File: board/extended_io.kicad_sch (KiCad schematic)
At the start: 54 parts, among them J5 I2C_3V3, Q10 BC548, Q11 BC548, Q12 BC548, Q13 BC548, Q14 BC548, Q15 BC548, Q16 BC548, Q17 BC548, Q18 BC548, Q7 BC548, Q8 BC548, Q9 BC548, SW11 TD_A, SW12 TD_B, SW13 TD2_A, SW14 TD2_B, SW15 SW_DIP_x03, U10 MCP23008-xP, U11 CAT24C256, U12 MCP7940N-xP, U9 24LC1025, Y1 32.768kHz

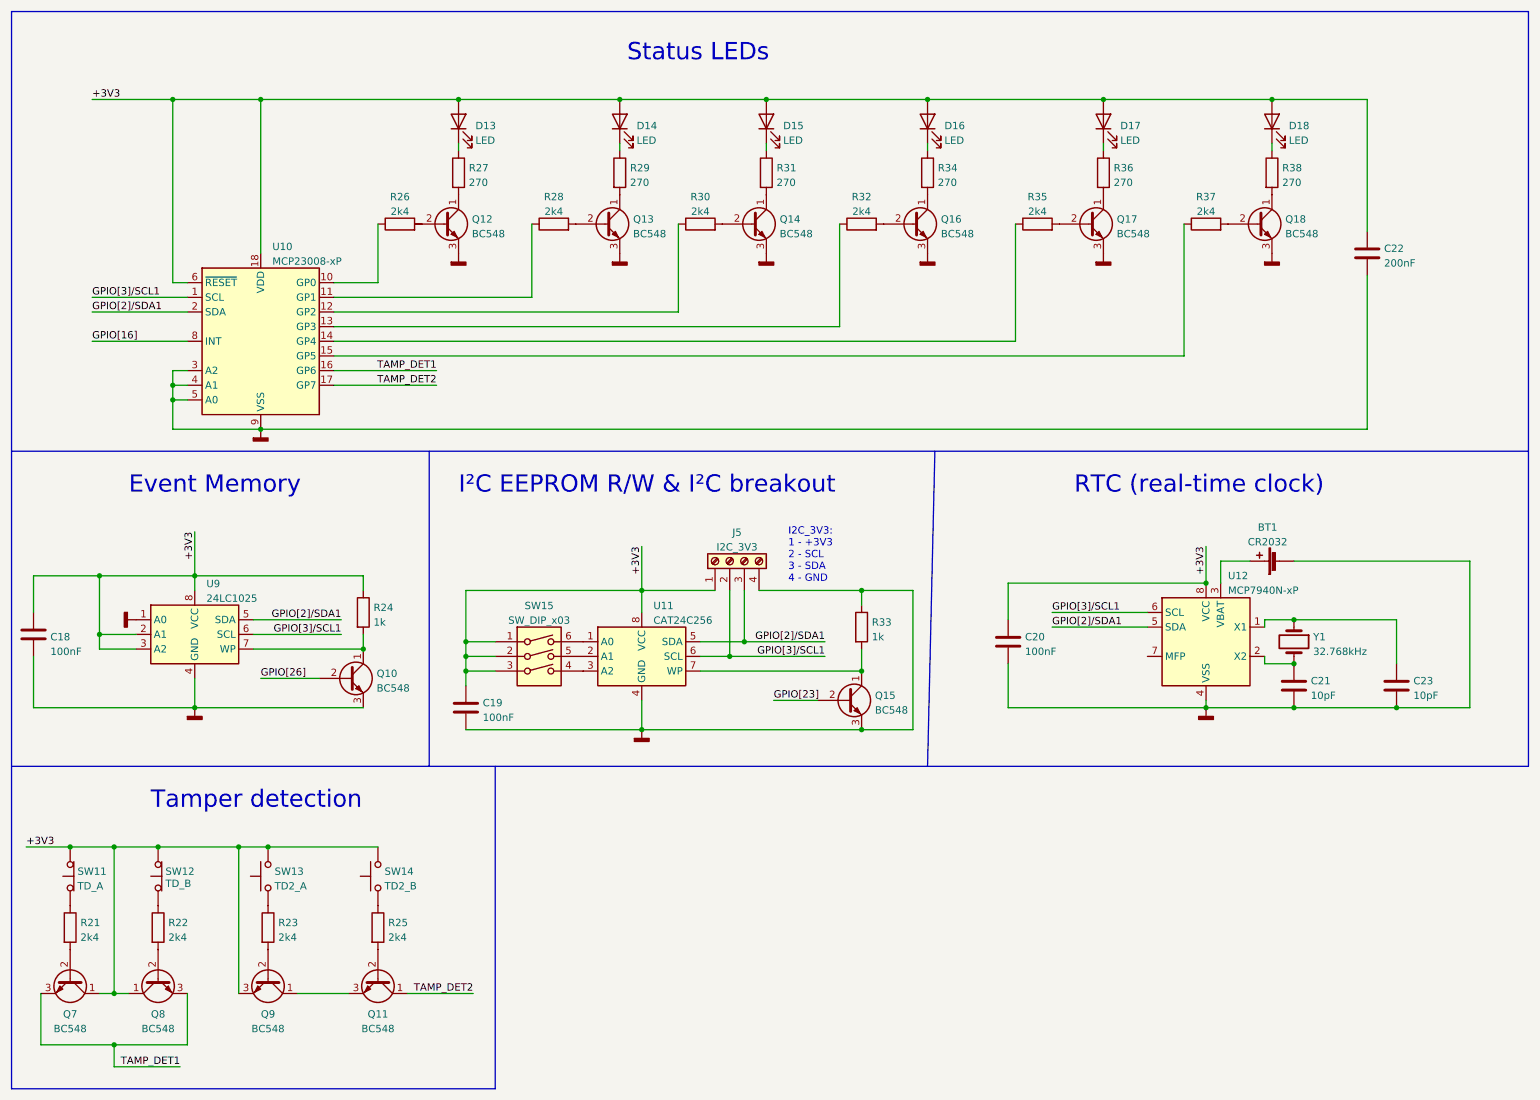
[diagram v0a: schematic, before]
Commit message: Improve power circuit and protection.
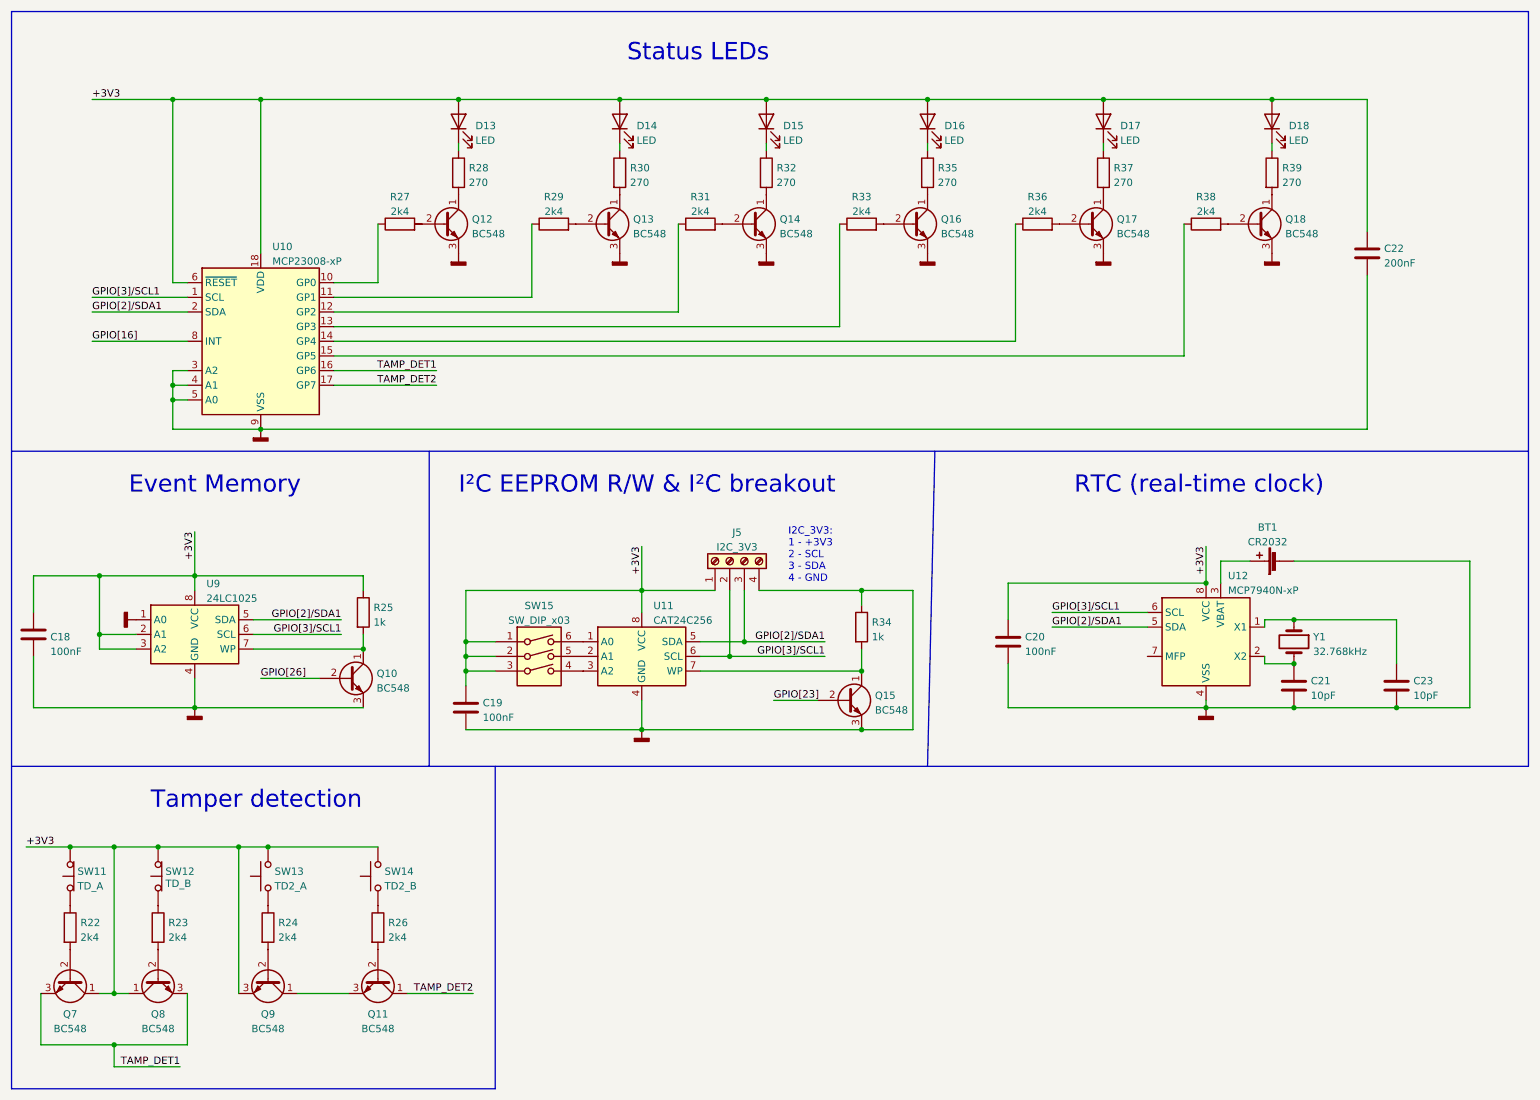
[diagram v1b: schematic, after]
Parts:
- renumbered R21 to R22, R22 to R23, R23 to R24, R24 to R25, R25 to R26, R26 to R27, R27 to R28, R28 to R29, R29 to R30, R30 to R31, R31 to R32, R32 to R33, R33 to R34, R34 to R35, R35 to R36, R36 to R37, R37 to R38, R38 to R39
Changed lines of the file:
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@@
   (symbol (lib_id "Device:R") (at 191.77 49.53 90) (unit 1)
     (in_bom yes) (on_board yes) (fields_autoplaced)
-    (property "Reference" "R35" (id 0) (at 191.77 44.8142 90))
+    (property "Reference" "R36" (id 0) (at 191.77 44.8142 90))
     (property "Value" "2k4" (id 1) (at 191.77 47.3511 90))
     (property "Footprint" "" (id 2) (at 191.77 51.308 90)
@@
   (symbol (lib_id "Device:R") (at 77.47 171.45 0) (unit 1)
     (in_bom yes) (on_board yes) (fields_autoplaced)
-    (property "Reference" "R25" (id 0) (at 79.248 170.6153 0)
+    (property "Reference" "R26" (id 0) (at 79.248 170.6153 0)
       (effects (font (size 1.27 1.27)) (justify left))
     )
@@
   (symbol (lib_id "Device:R") (at 161.29 49.53 90) (unit 1)
     (in_bom yes) (on_board yes) (fields_autoplaced)
-    (property "Reference" "R32" (id 0) (at 161.29 44.8142 90))
+    (property "Reference" "R33" (id 0) (at 161.29 44.8142 90))
     (property "Value" "2k4" (id 1) (at 161.29 47.3511 90))
     (property "Footprint" "" (id 2) (at 161.29 51.308 90)
@@
   (symbol (lib_id "Device:R") (at 24.13 171.45 0) (unit 1)
     (in_bom yes) (on_board yes) (fields_autoplaced)
-    (property "Reference" "R21" (id 0) (at 25.908 170.6153 0)
+    (property "Reference" "R22" (id 0) (at 25.908 170.6153 0)
       (effects (font (size 1.27 1.27)) (justify left))
     )
@@
   (symbol (lib_id "Device:R") (at 39.37 171.45 0) (unit 1)
     (in_bom yes) (on_board yes) (fields_autoplaced)
-    (property "Reference" "R22" (id 0) (at 41.148 170.6153 0)
+    (property "Reference" "R23" (id 0) (at 41.148 170.6153 0)
       (effects (font (size 1.27 1.27)) (justify left))
     )
@@
   (symbol (lib_id "Device:R") (at 91.44 40.64 0) (unit 1)
     (in_bom yes) (on_board yes) (fields_autoplaced)
-    (property "Reference" "R27" (id 0) (at 93.218 39.8053 0)
+    (property "Reference" "R28" (id 0) (at 93.218 39.8053 0)
       (effects (font (size 1.27 1.27)) (justify left))
     )
@@
   (symbol (lib_id "Device:R") (at 74.93 116.84 0) (unit 1)
     (in_bom yes) (on_board yes) (fields_autoplaced)
-    (property "Reference" "R24" (id 0) (at 76.708 116.0053 0)
+    (property "Reference" "R25" (id 0) (at 76.708 116.0053 0)
       (effects (font (size 1.27 1.27)) (justify left))
     )
@@
   (symbol (lib_id "Device:R") (at 203.2 40.64 0) (unit 1)
     (in_bom yes) (on_board yes) (fields_autoplaced)
-    (property "Reference" "R36" (id 0) (at 204.978 39.8053 0)
+    (property "Reference" "R37" (id 0) (at 204.978 39.8053 0)
       (effects (font (size 1.27 1.27)) (justify left))
     )
@@
   (symbol (lib_id "Device:R") (at 220.98 49.53 90) (unit 1)
     (in_bom yes) (on_board yes) (fields_autoplaced)
-    (property "Reference" "R37" (id 0) (at 220.98 44.8142 90))
+    (property "Reference" "R38" (id 0) (at 220.98 44.8142 90))
     (property "Value" "2k4" (id 1) (at 220.98 47.3511 90))
     (property "Footprint" "" (id 2) (at 220.98 51.308 90)
@@
   (symbol (lib_id "Device:R") (at 58.42 171.45 0) (unit 1)
     (in_bom yes) (on_board yes) (fields_autoplaced)
-    (property "Reference" "R23" (id 0) (at 60.198 170.6153 0)
+    (property "Reference" "R24" (id 0) (at 60.198 170.6153 0)
       (effects (font (size 1.27 1.27)) (justify left))
     )
@@
   (symbol (lib_id "Device:R") (at 81.28 49.53 90) (unit 1)
     (in_bom yes) (on_board yes) (fields_autoplaced)
-    (property "Reference" "R26" (id 0) (at 81.28 44.8142 90))
+    (property "Reference" "R27" (id 0) (at 81.28 44.8142 90))
     (property "Value" "2k4" (id 1) (at 81.28 47.3511 90))
     (property "Footprint" "" (id 2) (at 81.28 51.308 90)
@@
   (symbol (lib_id "Device:R") (at 144.78 40.64 0) (unit 1)
     (in_bom yes) (on_board yes) (fields_autoplaced)
-    (property "Reference" "R31" (id 0) (at 146.558 39.8053 0)
+    (property "Reference" "R32" (id 0) (at 146.558 39.8053 0)
       (effects (font (size 1.27 1.27)) (justify left))
     )
@@
   (symbol (lib_id "Device:R") (at 172.72 40.64 0) (unit 1)
     (in_bom yes) (on_board yes) (fields_autoplaced)
-    (property "Reference" "R34" (id 0) (at 174.498 39.8053 0)
+    (property "Reference" "R35" (id 0) (at 174.498 39.8053 0)
       (effects (font (size 1.27 1.27)) (justify left))
     )
@@
   (symbol (lib_id "Device:R") (at 133.35 49.53 90) (unit 1)
     (in_bom yes) (on_board yes) (fields_autoplaced)
-    (property "Reference" "R30" (id 0) (at 133.35 44.8142 90))
+    (property "Reference" "R31" (id 0) (at 133.35 44.8142 90))
     (property "Value" "2k4" (id 1) (at 133.35 47.3511 90))
     (property "Footprint" "" (id 2) (at 133.35 51.308 90)
@@
   (symbol (lib_id "Device:R") (at 161.29 119.38 0) (unit 1)
     (in_bom yes) (on_board yes) (fields_autoplaced)
-    (property "Reference" "R33" (id 0) (at 163.068 118.5453 0)
+    (property "Reference" "R34" (id 0) (at 163.068 118.5453 0)
       (effects (font (size 1.27 1.27)) (justify left))
     )
@@
   (symbol (lib_id "Device:R") (at 119.38 40.64 0) (unit 1)
     (in_bom yes) (on_board yes) (fields_autoplaced)
-    (property "Reference" "R29" (id 0) (at 121.158 39.8053 0)
+    (property "Reference" "R30" (id 0) (at 121.158 39.8053 0)
       (effects (font (size 1.27 1.27)) (justify left))
     )
@@
   (symbol (lib_id "Device:R") (at 232.41 40.64 0) (unit 1)
     (in_bom yes) (on_board yes) (fields_autoplaced)
-    (property "Reference" "R38" (id 0) (at 234.188 39.8053 0)
+    (property "Reference" "R39" (id 0) (at 234.188 39.8053 0)
       (effects (font (size 1.27 1.27)) (justify left))
     )
@@
   (symbol (lib_id "Device:R") (at 107.95 49.53 90) (unit 1)
     (in_bom yes) (on_board yes) (fields_autoplaced)
-    (property "Reference" "R28" (id 0) (at 107.95 44.8142 90))
+    (property "Reference" "R29" (id 0) (at 107.95 44.8142 90))
     (property "Value" "2k4" (id 1) (at 107.95 47.3511 90))
     (property "Footprint" "" (id 2) (at 107.95 51.308 90)
